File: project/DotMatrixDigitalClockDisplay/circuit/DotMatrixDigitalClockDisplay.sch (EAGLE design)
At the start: 83 parts

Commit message: 回路作成中
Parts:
- IC1, IC2: value (none) -> PIC16F886
- IC3, IC4: value (none) -> TBD62083APG
- Q1, Q2: value (none) -> 20MHz
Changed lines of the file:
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@@
 <?xml version="1.0" encoding="utf-8"?>
 <!DOCTYPE eagle SYSTEM "eagle.dtd">
-<eagle version="9.6.2">
+<eagle version="9.6.1">
 <drawing>
 <settings>
@@
 <part name="R12" library="rcl" library_urn="urn:adsk.eagle:library:334" deviceset="R-EU_" device="0207/2V" package3d_urn="urn:adsk.eagle:package:23490/1" value="100"/>
 <part name="R13" library="rcl" library_urn="urn:adsk.eagle:library:334" deviceset="R-EU_" device="0207/2V" package3d_urn="urn:adsk.eagle:package:23490/1" value="100"/>
-<part name="IC1" library="ic-package" library_urn="urn:adsk.eagle:library:239" deviceset="DIL28" device="-3" package3d_urn="urn:adsk.eagle:package:827/2"/>
-<part name="IC2" library="ic-package" library_urn="urn:adsk.eagle:library:239" deviceset="DIL28" device="-3" package3d_urn="urn:adsk.eagle:package:827/2"/>
-<part name="IC3" library="ic-package" library_urn="urn:adsk.eagle:library:239" deviceset="DIL18" device="" package3d_urn="urn:adsk.eagle:package:16424/2"/>
+<part name="IC1" library="ic-package" library_urn="urn:adsk.eagle:library:239" deviceset="DIL28" device="-3" package3d_urn="urn:adsk.eagle:package:827/2" value="PIC16F886"/>
+<part name="IC2" library="ic-package" library_urn="urn:adsk.eagle:library:239" deviceset="DIL28" device="-3" package3d_urn="urn:adsk.eagle:package:827/2" value="PIC16F886"/>
+<part name="IC3" library="ic-package" library_urn="urn:adsk.eagle:library:239" deviceset="DIL18" device="" package3d_urn="urn:adsk.eagle:package:16424/2" value="TBD62083APG"/>
 <part name="P+1" library="supply1" library_urn="urn:adsk.eagle:library:371" deviceset="+5V" device=""/>
 <part name="GND2" library="supply1" library_urn="urn:adsk.eagle:library:371" deviceset="GND" device=""/>
-<part name="Q1" library="murata-resonators" deviceset="CSTLS_X" device=""/>
+<part name="Q1" library="murata-resonators" deviceset="CSTLS_X" device="" value="20MHz"/>
 <part name="GND1" library="supply1" library_urn="urn:adsk.eagle:library:371" deviceset="GND" device=""/>
-<part name="IC4" library="ic-package" library_urn="urn:adsk.eagle:library:239" deviceset="DIL18" device="" package3d_urn="urn:adsk.eagle:package:16424/2"/>
+<part name="IC4" library="ic-package" library_urn="urn:adsk.eagle:library:239" deviceset="DIL18" device="" package3d_urn="urn:adsk.eagle:package:16424/2" value="TBD62083APG"/>
 <part name="GND3" library="supply1" library_urn="urn:adsk.eagle:library:371" deviceset="GND" device=""/>
 <part name="P+2" library="supply1" library_urn="urn:adsk.eagle:library:371" deviceset="+5V" device=""/>
-<part name="Q2" library="murata-resonators" deviceset="CSTLS_X" device=""/>
+<part name="Q2" library="murata-resonators" deviceset="CSTLS_X" device="" value="20MHz"/>
 <part name="GND4" library="supply1" library_urn="urn:adsk.eagle:library:371" deviceset="GND" device=""/>
 <part name="SV2" library="con-lstb" library_urn="urn:adsk.eagle:library:162" deviceset="MA06-1" device="" package3d_urn="urn:adsk.eagle:package:8340/1"/>

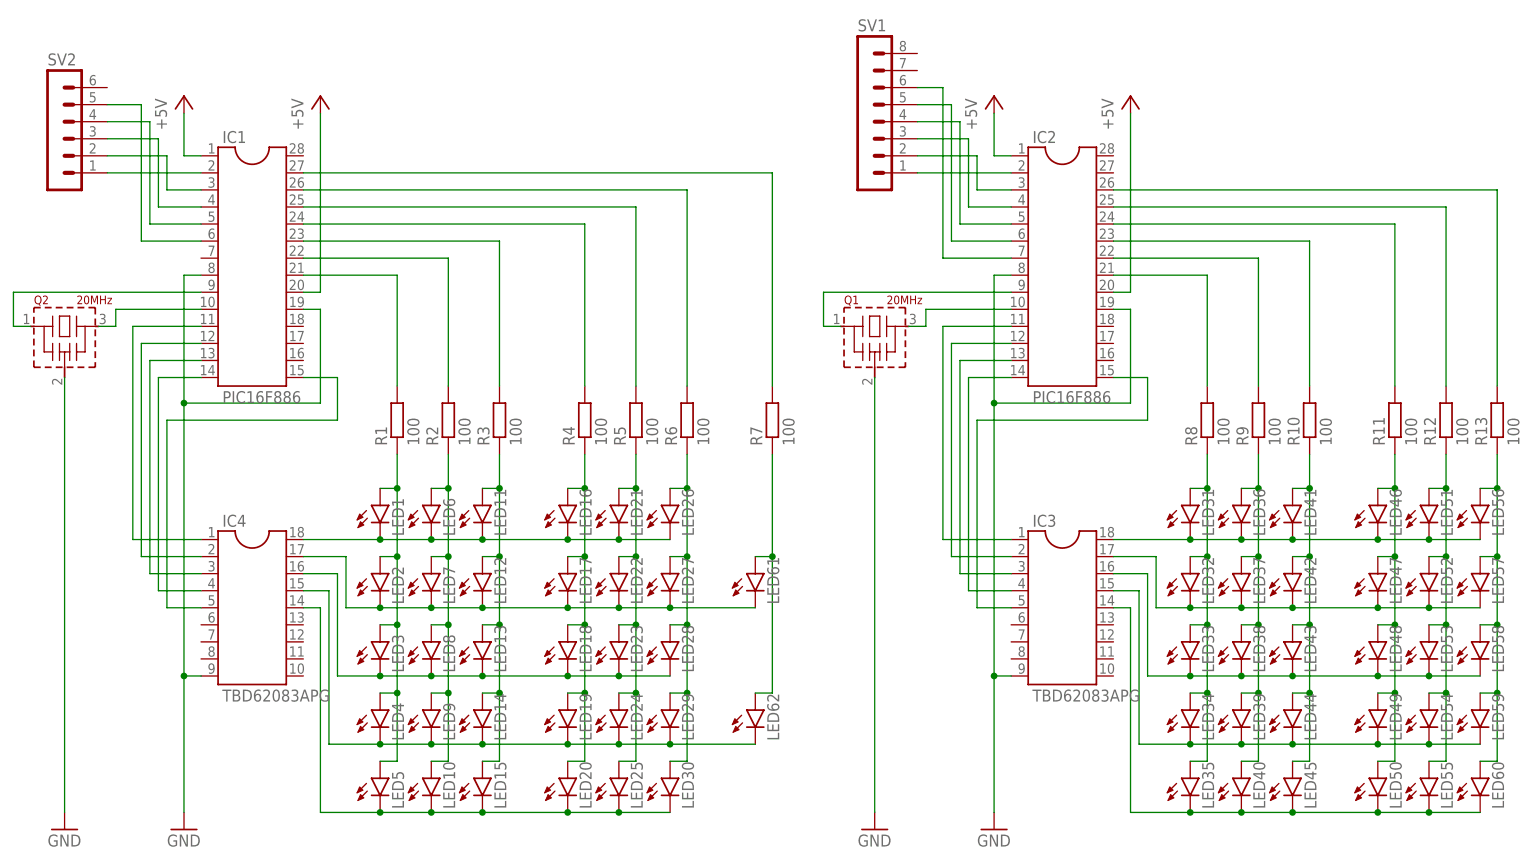
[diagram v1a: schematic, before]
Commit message: DotMatrixDigitalClockDisplayの回路を作成
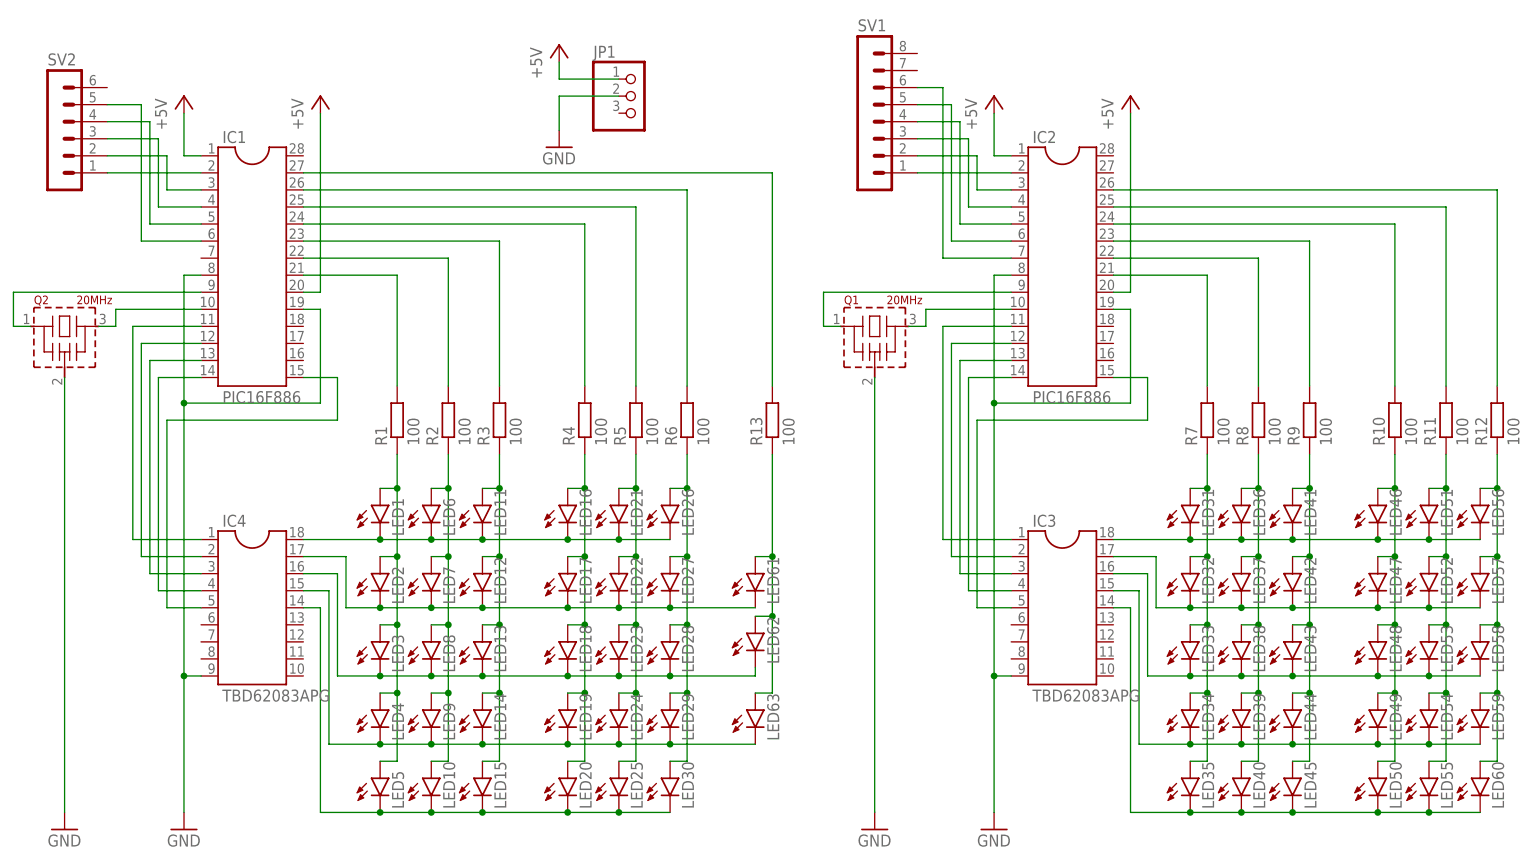
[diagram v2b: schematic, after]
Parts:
- added JP1: (no value), pinhead:PINHD-1X3
- added LED63: (no value), led:LED5MM
- R1, R10, R11, R12, R13, R2, R3, R4, R5, R6, R7, R8, R9: device rcl:R-EU_0207/2V -> rcl:R-EU_0207/7
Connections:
- net +5V: now also JP1.1
- net GND: now also JP1.2
- net N$10: now also R10.1; no longer R11.1
- net N$11: now also R11.1; no longer R12.1
- net N$12: now also R12.1; no longer R13.1
- net N$13: now also LED63.A, R13.1; no longer R7.1
- net N$16: now also LED62.C
- net N$17: now also LED63.C; no longer LED62.C
- net N$29: now also R7.2; no longer R8.2
- net N$30: now also R8.2; no longer R9.2
- net N$31: now also R9.2; no longer R10.2
- net N$32: now also R10.2; no longer R11.2
- net N$33: now also R11.2; no longer R12.2
- net N$34: now also R12.2; no longer R13.2
- net N$48: now also R13.2; no longer R7.2
- net N$7: now also R7.1; no longer R8.1
- net N$8: now also R8.1; no longer R9.1
- net N$9: now also R9.1; no longer R10.1
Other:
- moved on the sheet: LED62, R10, R11, R12, R13, R7, R8, R9
